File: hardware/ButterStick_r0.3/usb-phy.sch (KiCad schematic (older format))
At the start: 13 parts, among them J10 USB_C_Receptacle_USB2.0, U14 USB3343

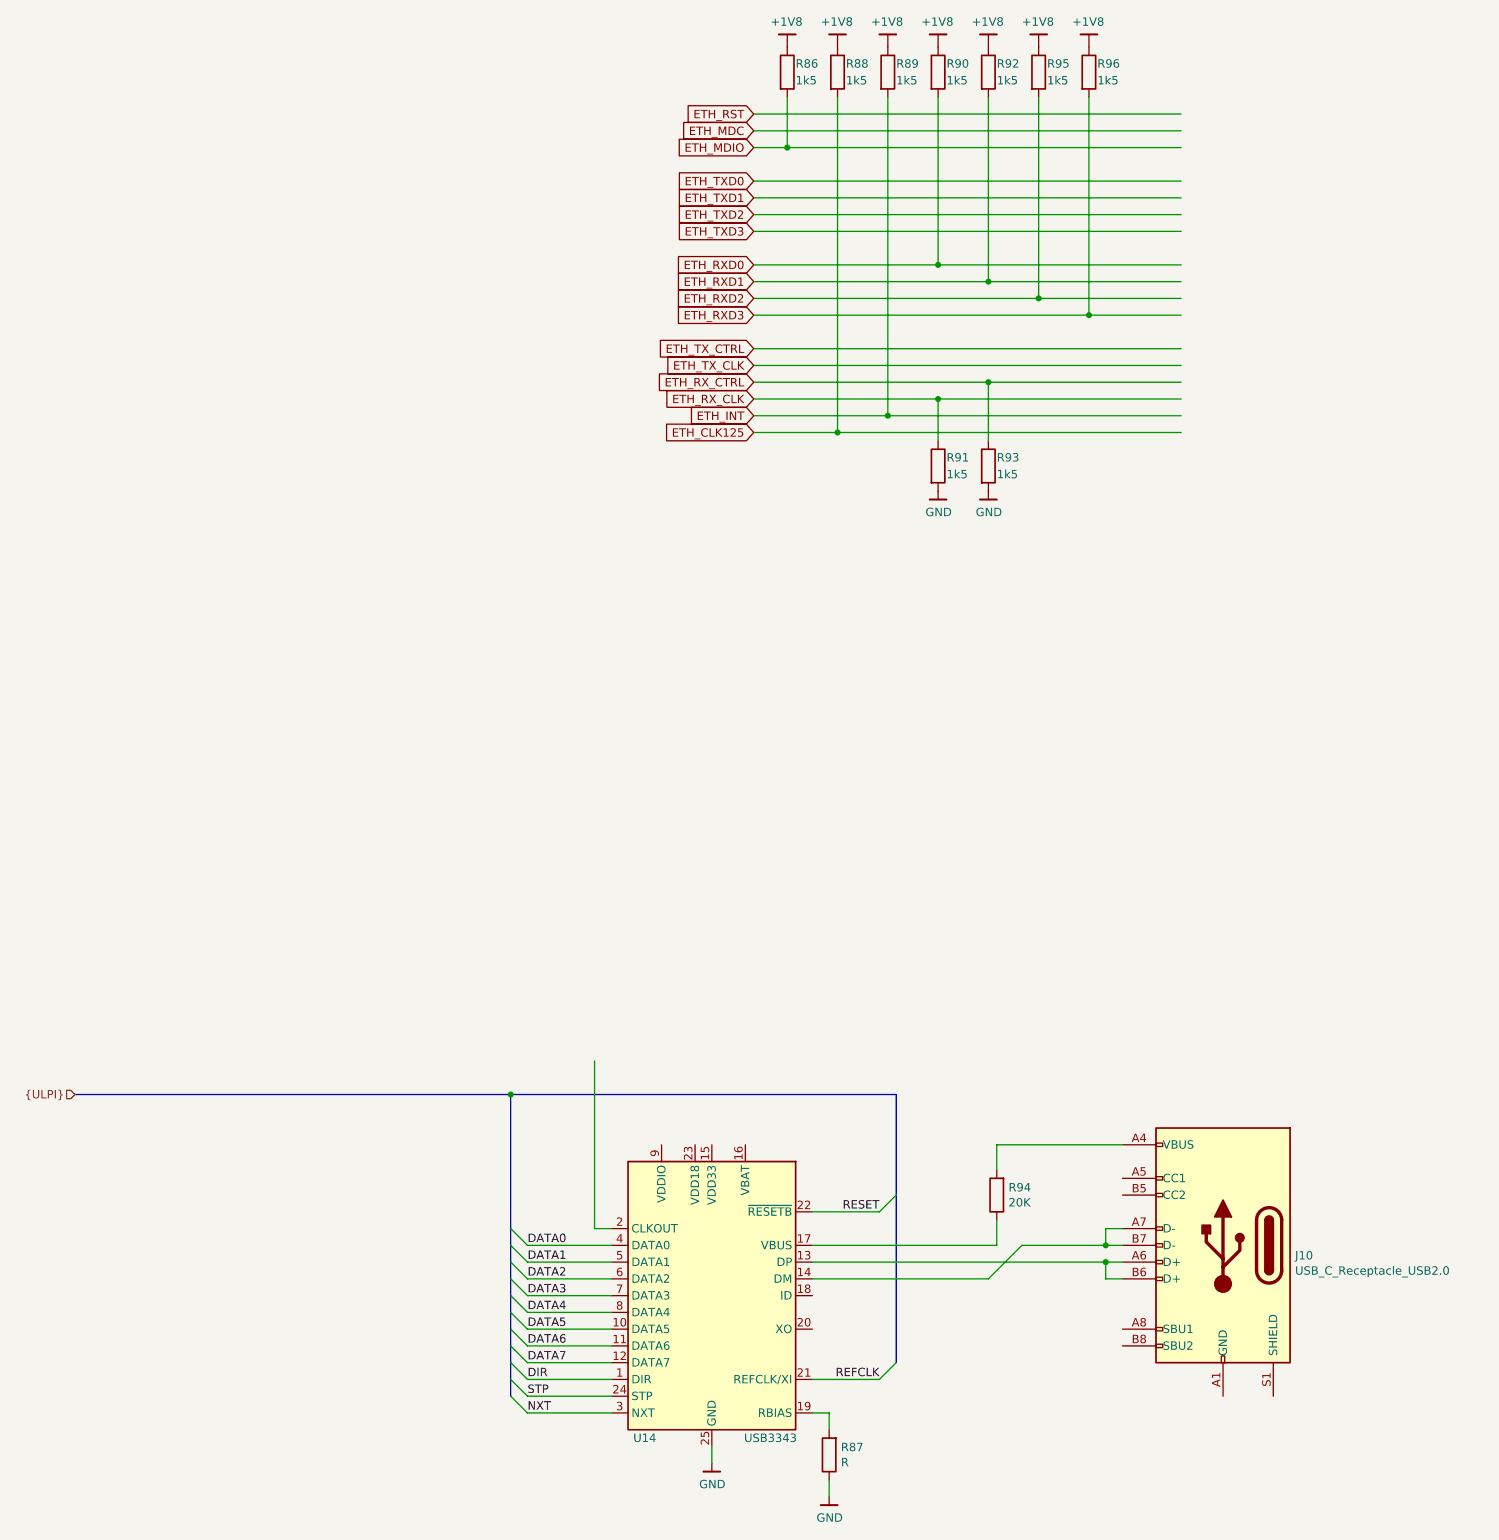
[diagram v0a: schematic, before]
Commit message: hw.r0_3: Update schematics with 85F-5G symbol
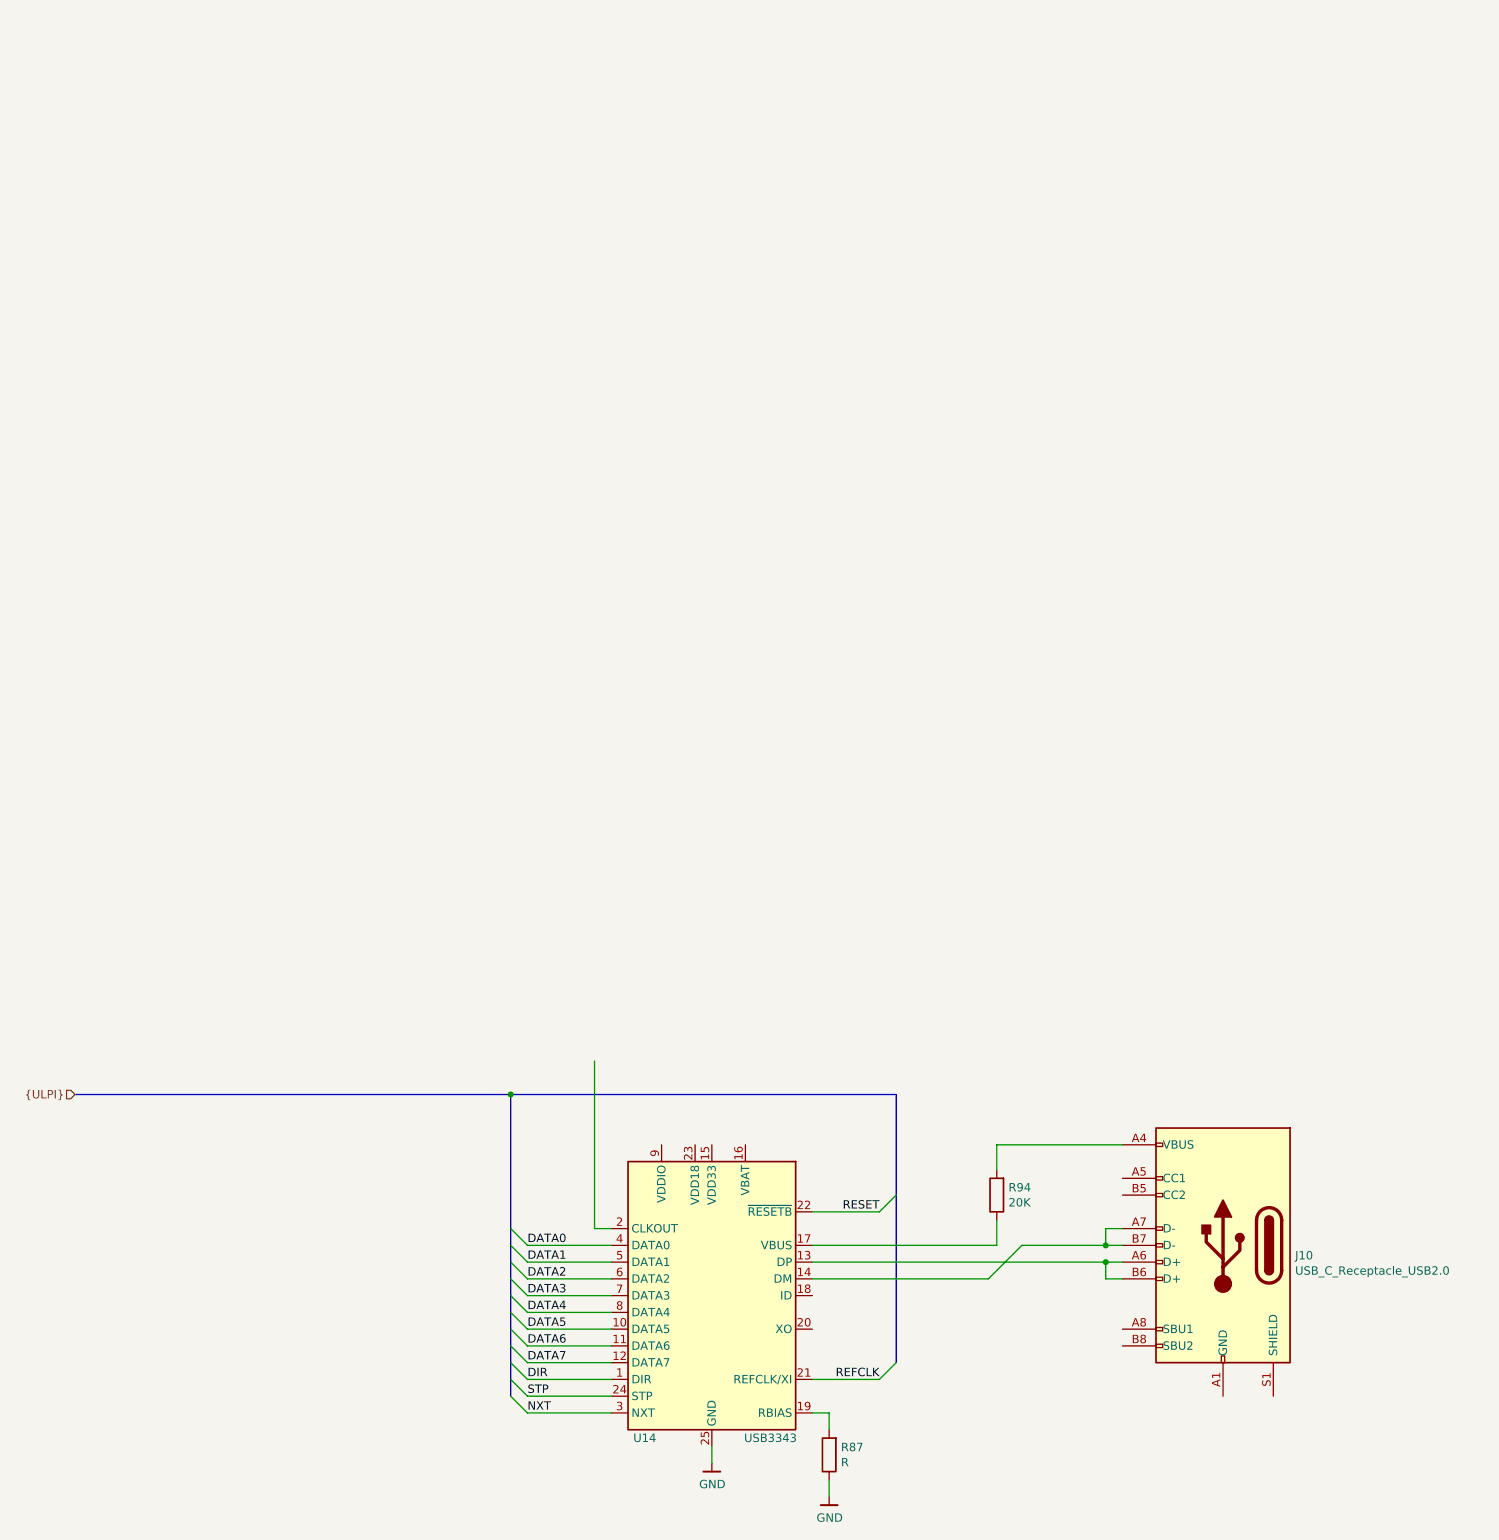
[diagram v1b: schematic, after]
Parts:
- removed R86, R88, R89, R90, R91, R92, R93, R95, R96: 1k5, Resistor_SMD:R_0402_1005Metric, symbol Device:R
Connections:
- net labels removed: +1V8, ETH_CLK125, ETH_INT, ETH_MDC, ETH_MDIO, ETH_RST, ETH_RXD0, ETH_RXD1, ETH_RXD2, ETH_RXD3, ETH_RX_CLK, ETH_RX_CTRL, ETH_TXD0, ETH_TXD1, ETH_TXD2, ETH_TXD3, ETH_TX_CLK, ETH_TX_CTRL
- wire segments 68 -> 33
